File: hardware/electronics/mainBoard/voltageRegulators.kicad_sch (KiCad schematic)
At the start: 46 parts, among them U16 TPS543B25, U17 TPS62A01, U18 TPS62A01, U19 TPS629206

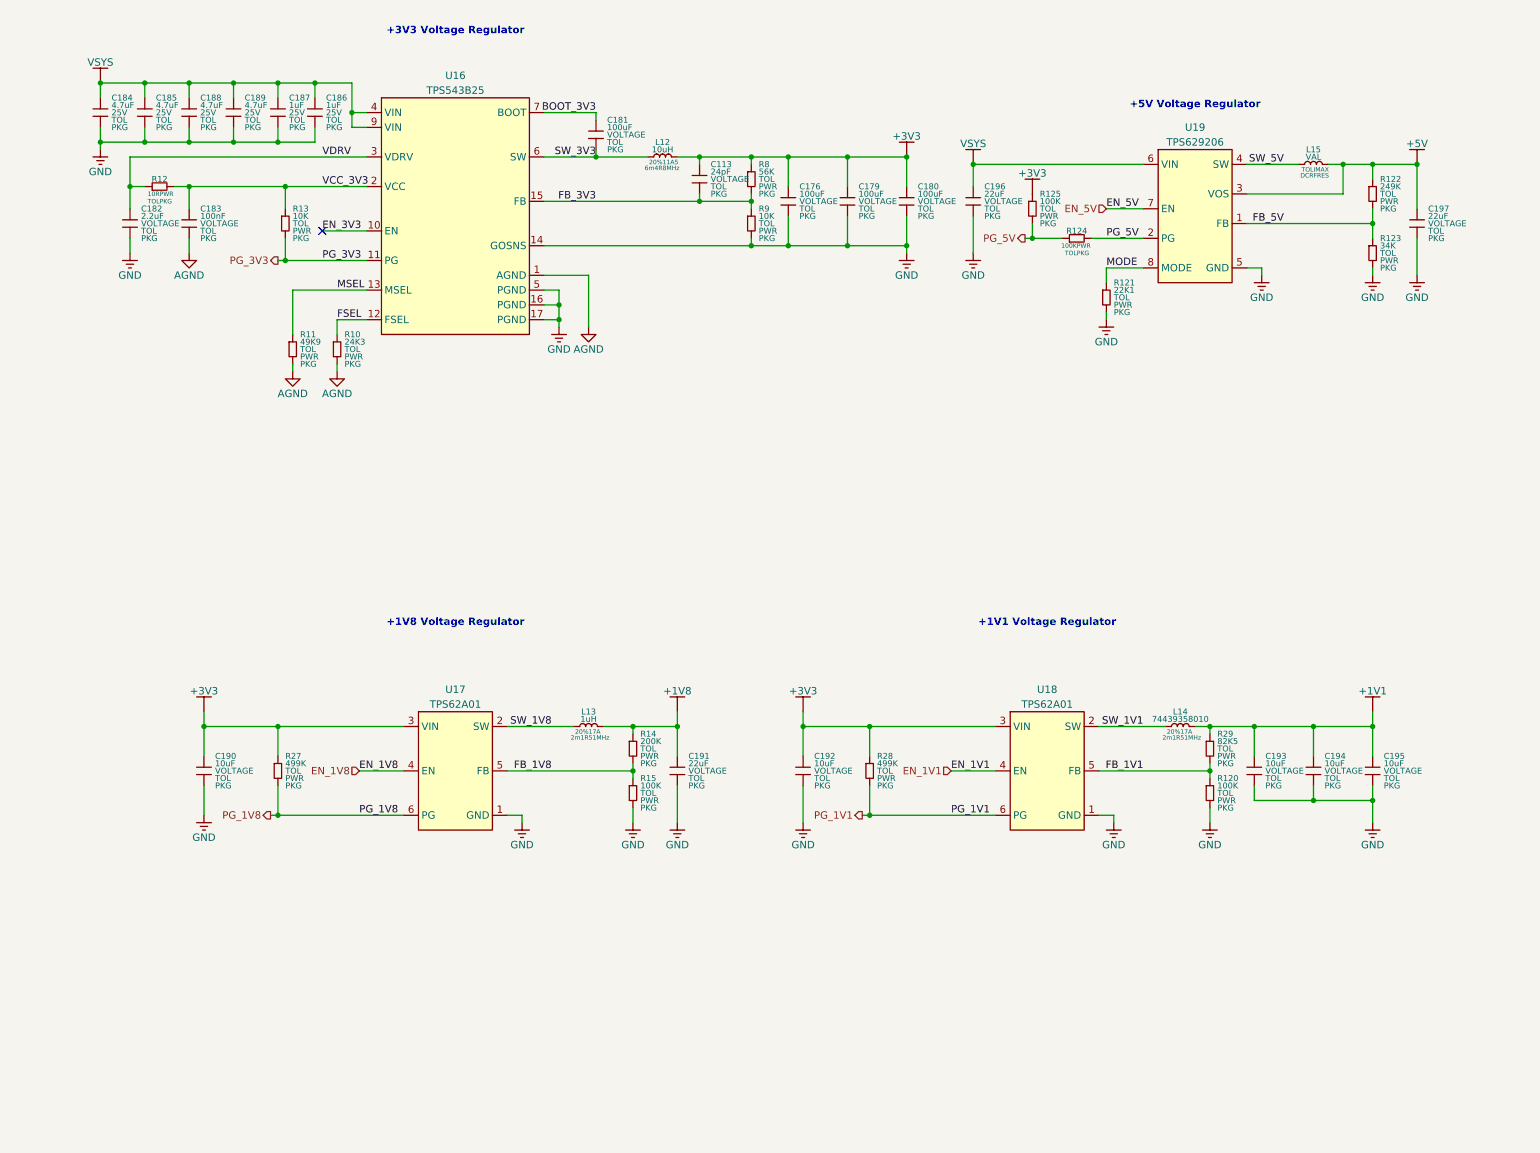
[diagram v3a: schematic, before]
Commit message: added part numbers and stuff
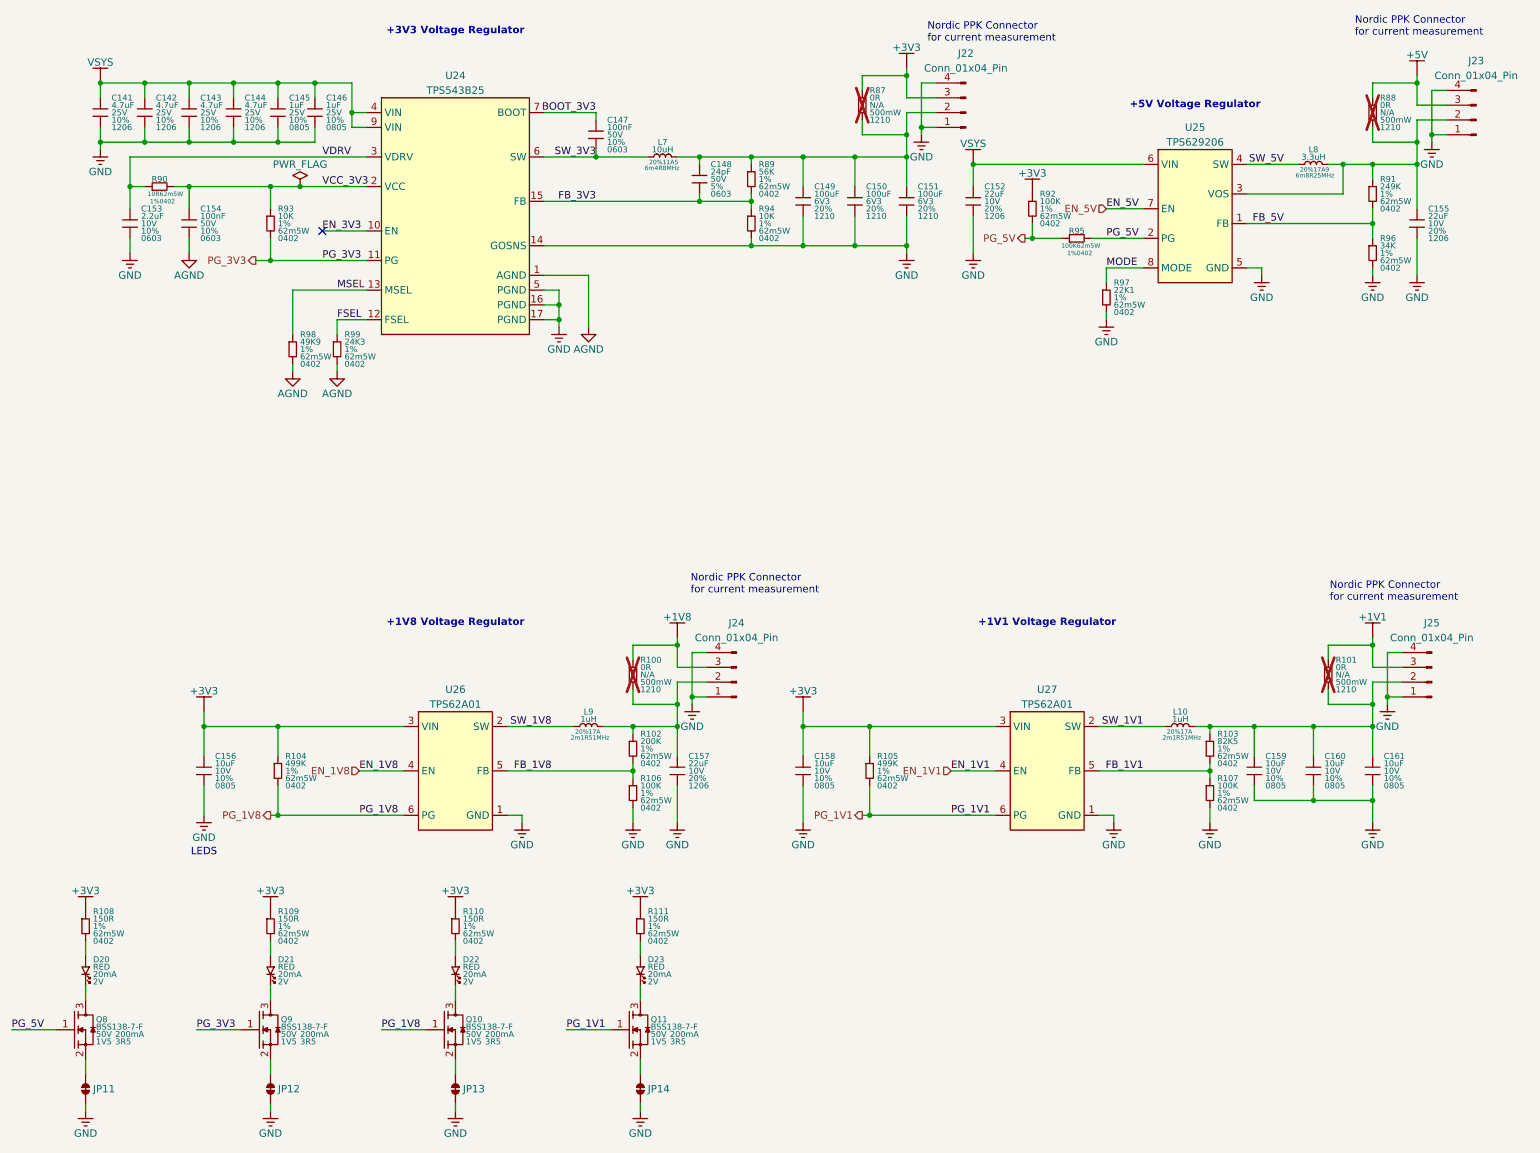
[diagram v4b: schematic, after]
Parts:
- removed C179, C180, C181: 100uF, symbol lib_sch:C
- removed C183: 100nF, symbol lib_sch:C
- removed C185, C188, C189: 4.7uF, symbol lib_sch:C
- removed C186: 1uF, symbol lib_sch:C
- removed C190, C192, C193, C194, C195: 10uF, symbol lib_sch:C
- removed C191, C196, C197: 22uF, symbol lib_sch:C
- removed R120, R15: 100K, symbol lib_sch:R
- removed R13, R9: 10K, symbol lib_sch:R
- removed R28: 499K, symbol lib_sch:R
- added C142, C143, C144: 4.7uF, symbol lib_sch:C
- added C146: 1uF, symbol lib_sch:C
- added C147, C154: 100nF, symbol lib_sch:C
- added C150, C151: 100uF, symbol lib_sch:C
- added C152, C155, C157: 22uF, symbol lib_sch:C
- added C156, C158, C159, C160, C161: 10uF, symbol lib_sch:C
- added D20, D21, D22, D23: LTST-C191KRKT, symbol lib_sch:LED
- added J22, J23, J24, J25: Conn_01x04_Pin, symbol lib_sch:Conn_01x04_Pin
- added JP11, JP12, JP13, JP14: ~, symbol lib_sch:Jumper_2_Bridged
- added Q10, Q11, Q8, Q9: BSS138-7-F, symbol .DS-Transistors:NMOS_GSD
- added R100, R101, R87, R88: 0R, symbol lib_sch:R
- added R105: 499K, symbol lib_sch:R
- added R106, R107: 100K, symbol lib_sch:R
- added R108, R109, R110, R111: 150R, symbol lib_sch:R
- added R93, R94: 10K, symbol lib_sch:R
- C141: renamed from C184; DKPN (none) -> 478-KAM31GR71E475KLCT-ND; MPN (none) -> 12063C475K4T4A; Manufacturer (none) -> KYOCERA AVX; Package PKG -> 1206; Tolerance TOL -> 10%
- C145: renamed from C187; DKPN (none) -> 478-KAF21KR71E105KLCT-ND; MPN (none) -> 08053C105K4Z4A; Manufacturer (none) -> KYOCERA AVX; Package PKG -> 0805; Tolerance TOL -> 10%
- C148: renamed from C113; DKPN (none) -> 478-10304-1-ND; MPN (none) -> 06035A240JAT2A; Manufacturer (none) -> KYOCERA AVX; Package PKG -> 0603; Tolerance TOL -> 5%; Voltage Rating VOLTAGE -> 50V
- C149: renamed from C176; DKPN (none) -> 490-GRT32EC70J107ME13LCT-ND; MPN (none) -> GRT32EC70J107ME13L; Manufacturer (none) -> Murata Electronics; Package PKG -> 1210; Tolerance TOL -> 20%; Voltage Rating VOLTAGE -> 6V3
- C153: renamed from C182; DKPN (none) -> 478-KAM15AR71A225KTCT-ND; MPN (none) -> KAM15AR71A225KT; Manufacturer (none) -> KYOCERA AVX; Package PKG -> 0603; Tolerance TOL -> 10%; Voltage Rating VOLTAGE -> 10V
- L10: renamed from L14; value 74439358010 -> 1uH
- L8: renamed from L15; value VAL -> 3.3uH; Current Rating IMAX -> 17A9; DC Resistance DCR -> 6m8R; DKPN (none) -> 732-74439358033CT-ND; MPN (none) -> 74439358033; Manufacturer (none) -> Würth Elektronik; Resonant Frequency FRES -> 25MHz; Tolerance TOL -> 20%
- R102: renamed from R14; DKPN (none) -> 541-200KLCT-ND; MPN (none) -> CRCW0402200KFKED; Manufacturer (none) -> Vishay Dale; Package PKG -> 0402; Power Rating PWR -> 62m5W; Tolerance TOL -> 1%
- R103: renamed from R29; DKPN (none) -> 541-82.5KLCT-ND; MPN (none) -> CRCW040282K5FKED; Manufacturer (none) -> Vishay Dale; Package PKG -> 0402; Power Rating PWR -> 62m5W; Tolerance TOL -> 1%
- R104: renamed from R27; DKPN (none) -> 541-499KLCT-ND; MPN (none) -> CRCW0402499KFKED; Manufacturer (none) -> Vishay Dale; Package PKG -> 0402; Power Rating PWR -> 62m5W; Tolerance TOL -> 1%
- R89: renamed from R8; DKPN (none) -> 541-56.0KLCT-ND; MPN (none) -> CRCW040256K0FKED; Manufacturer (none) -> Vishay Dale; Package PKG -> 0402; Power Rating PWR -> 62m5W; Tolerance TOL -> 1%
- R90: renamed from R12; DKPN (none) -> 541-10.0LCT-ND; MPN (none) -> CRCW040210R0FKED; Manufacturer (none) -> Vishay Dale; Package PKG -> 0402; Power Rating PWR -> 62m5W; Tolerance TOL -> 1%
- R91: renamed from R122; DKPN (none) -> 541-249KLCT-ND; MPN (none) -> CRCW0402249KFKED; Manufacturer (none) -> Vishay Dale; Package PKG -> 0402; Power Rating PWR -> 62m5W; Tolerance TOL -> 1%
- R92: renamed from R125; DKPN (none) -> 541-100KLCT-ND; MPN (none) -> CRCW0402100KFKED; Manufacturer (none) -> Vishay Dale; Package PKG -> 0402; Power Rating PWR -> 62m5W; Tolerance TOL -> 1%
- R95: renamed from R124; DKPN (none) -> 541-100KLCT-ND; MPN (none) -> CRCW0402100KFKED; Manufacturer (none) -> Vishay Dale; Package PKG -> 0402; Power Rating PWR -> 62m5W; Tolerance TOL -> 1%
- R96: renamed from R123; DKPN (none) -> 541-34.0KLCT-ND; MPN (none) -> CRCW040234K0FKED; Manufacturer (none) -> Vishay Dale; Package PKG -> 0402; Power Rating PWR -> 62m5W; Tolerance TOL -> 1%
- R97: renamed from R121; DKPN (none) -> 541-22.1KLCT-ND; MPN (none) -> CRCW040222K1FKED; Manufacturer (none) -> Vishay Dale; Package PKG -> 0402; Power Rating PWR -> 62m5W; Tolerance TOL -> 1%
- R98: renamed from R11; DKPN (none) -> 541-49.9KLCT-ND; MPN (none) -> CRCW040249K9FKED; Manufacturer (none) -> Vishay Dale; Package PKG -> 0402; Power Rating PWR -> 62m5W; Tolerance TOL -> 1%
- R99: renamed from R10; DKPN (none) -> 541-24.3KLCT-ND; MPN (none) -> CRCW040224K3FKED; Manufacturer (none) -> Vishay Dale; Package PKG -> 0402; Power Rating PWR -> 62m5W; Tolerance TOL -> 1%
- U24: renamed from U16; symbol .DS-PMIC:TPS543B25 -> lib_sch:TPS543B25
- U25: renamed from U19; symbol .DS-PMIC:TPS629206 -> lib_sch:TPS629206; DKPN (none) -> 296-TPS629206DRLRCT-ND; MPN (none) -> TPS629206DRLR
- U26: renamed from U17; symbol .DS-PMIC:TPS62A0x -> lib_sch:TPS62A0x
- U27: renamed from U18; symbol .DS-PMIC:TPS62A0x -> lib_sch:TPS62A0x
- renumbered L12 to L7, L13 to L9
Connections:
- net +1V1: now also J25.3 (Pin_3), R101.1; no longer L10.2, R103.1
- net +1V8: now also J24.3 (Pin_3), R100.1; no longer L9.2, R102.1
- net +3V3: now also C156.1, C158.1, J22.3 (Pin_3), R105.1, R108.1, R109.1, R110.1, R111.1, R87.1; no longer C148.1, C149.1, L7.2, R89.1
- net +5V: now also J23.3 (Pin_3), R88.1; no longer L8.2, R91.1, U25.3 (VOS)
- net AGND: now also C154.2
- net BOOT_3V3: now also C147.1
- net FB_1V1: now also R107.1
- net FB_1V8: now also R106.1
- net FB_3V3: now also R94.1
- net GND: now also C142.2, C143.2, C144.2, C146.2, C150.2, C151.2, C152.2, C155.2, C156.2, C157.2, C158.2, C159.2, C160.2, C161.2, J22.1 (Pin_1), J22.4 (Pin_4), J23.1 (Pin_1), J23.4 (Pin_4), J24.1 (Pin_1), J24.4 (Pin_4), J25.1 (Pin_1), J25.4 (Pin_4), JP11.2, JP12.2, JP13.2, JP14.2, R106.2, R107.2, R94.2
- net PG_1V1: now also Q11.1, R105.2
- net PG_1V8: now also Q10.1
- net PG_3V3: now also Q9.1, R93.2
- net PG_5V: now also Q8.1
- net SW_3V3: now also C147.2
- net VCC_3V3: now also C154.1, R93.1
- net VSYS: now also C142.1, C143.1, C144.1, C146.1, C152.1
- new net: D22.1, R110.2
- new net: D22.2, Q10.3
- new net: C155.1, J23.2 (Pin_2), L8.2, R88.2, R91.1, U25.3 (VOS)
- new net: C159.1, C160.1, C161.1, J25.2 (Pin_2), L10.2, R101.2, R103.1
- new net: C148.1, C149.1, C150.1, C151.1, J22.2 (Pin_2), L7.2, R87.2, R89.1
- new net: JP14.1, Q11.2
- new net: C157.1, J24.2 (Pin_2), L9.2, R100.2, R102.1
- new net: D21.1, R109.2
- new net: D21.2, Q9.3
- new net: JP13.1, Q10.2
- new net: JP12.1, Q9.2
- new net: D20.1, R108.2
- new net: D20.2, Q8.3
- new net: D23.2, Q11.3
- new net: JP11.1, Q8.2
- new net: D23.1, R111.2
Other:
- note added: "LEDS"
- note added: "Nordic PPK Connector for current measurement"
- moved on the sheet: C149

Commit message: got rid of 5V and 1V1 regs
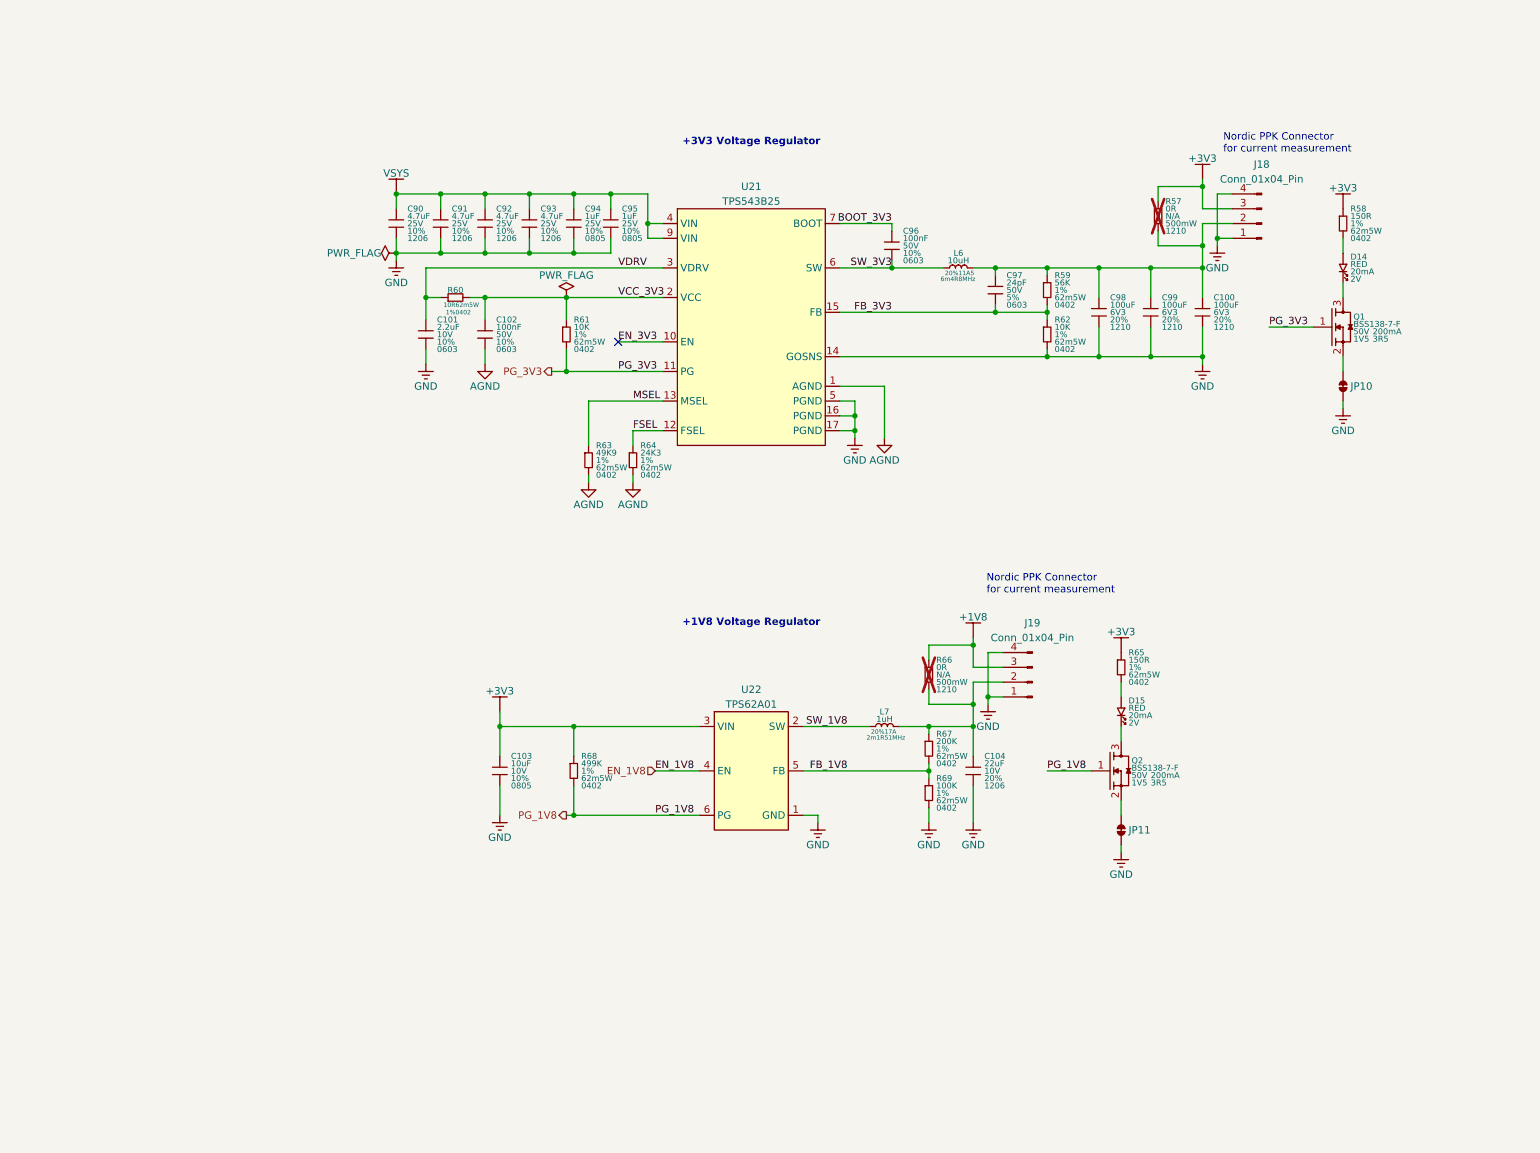
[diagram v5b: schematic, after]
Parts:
- removed C152, C155: 22uF, symbol lib_sch:C
- removed C158, C159, C160, C161: 10uF, symbol lib_sch:C
- removed D20, D23: LTST-C191KRKT, symbol lib_sch:LED
- removed J23, J24, J25: Conn_01x04_Pin, symbol lib_sch:Conn_01x04_Pin
- removed JP11, JP14: ~, symbol lib_sch:Jumper_2_Bridged
- removed L10: 1uH, symbol lib_sch:L_horizontal
- removed L8: 3.3uH, symbol lib_sch:L_horizontal
- removed Q11, Q8: BSS138-7-F, symbol .DS-Transistors:NMOS_GSD
- removed R101, R88: 0R, symbol lib_sch:R
- removed R103: 82K5, symbol lib_sch:R
- removed R105: 499K, symbol lib_sch:R
- removed R107, R92: 100K, symbol lib_sch:R
- removed R108, R111: 150R, symbol lib_sch:R
- removed R91: 249K, symbol lib_sch:R
- removed R95: 100K, symbol lib_sch:R_horizontal
- removed R96: 34K, symbol lib_sch:R
- removed R97: 22K1, symbol lib_sch:R
- removed U25: TPS629206, symbol lib_sch:TPS629206
- removed U27: TPS62A01, symbol lib_sch:TPS62A0x
- added J19: Conn_01x04_Pin, symbol lib_sch:Conn_01x04_Pin
- renumbered C151 to C100, C153 to C101, C154 to C102, C156 to C103, C157 to C104, C141 to C90, C142 to C91, C143 to C92, C144 to C93, C145 to C94, C146 to C95, C147 to C96, C148 to C97, C149 to C98, C150 to C99, D21 to D14, D22 to D15, J22 to J18, JP12 to JP10, JP13 to JP11, L7 to L6, L9 to L7, Q9 to Q1, Q10 to Q2, R87 to R57, R109 to R58, R89 to R59, R90 to R60, R93 to R61, R94 to R62, R98 to R63, R99 to R64, R110 to R65, R100 to R66, R102 to R67, R104 to R68, R106 to R69, U24 to U21, U26 to U22
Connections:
- net +1V8: now also J19.3 (Pin_3)
- net GND: now also J19.1 (Pin_1), J19.4 (Pin_4)
- net at C104.1, L7.2, R66.2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: now also J19.2 (Pin_2)
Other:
- note removed: "+1V1 Voltage Regulator"
- note removed: "+5V Voltage Regulator"
- note removed: "LEDS"
- moved on the sheet: C100, C101, C102, C103, C104, C90, C91, C92, C93, C94, C95, C96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

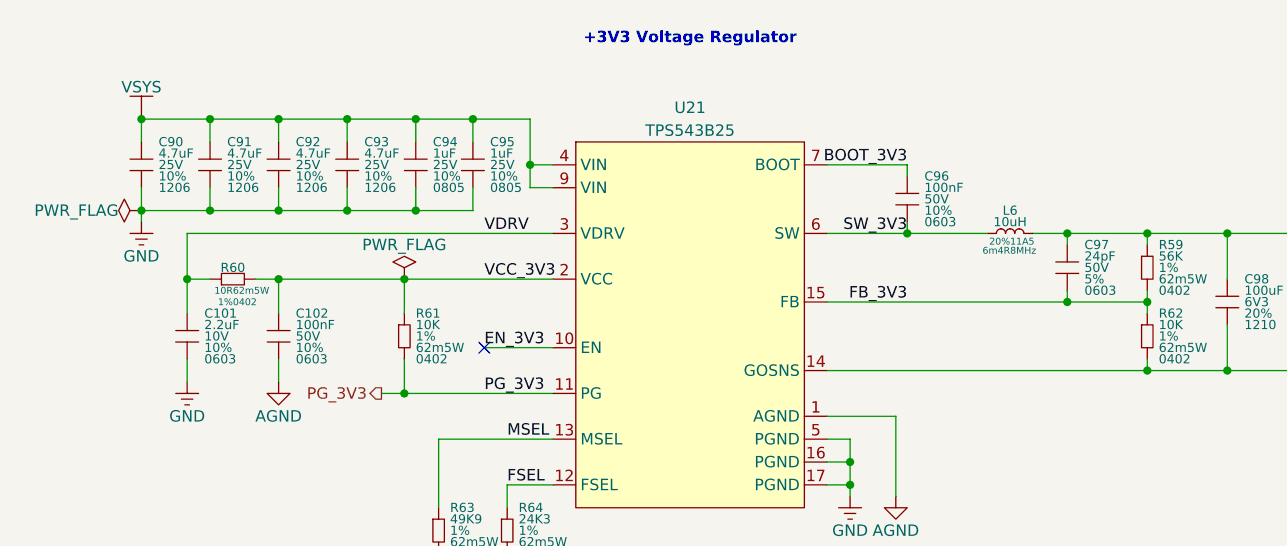
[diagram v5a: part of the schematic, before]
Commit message: updated capacitors
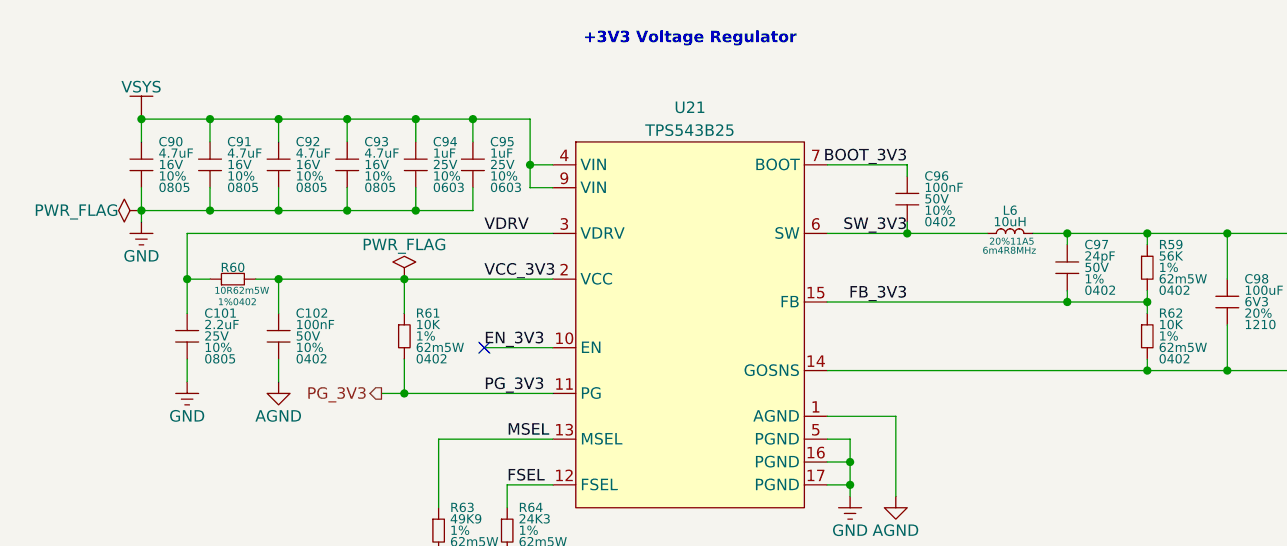
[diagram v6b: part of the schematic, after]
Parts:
- C101: DKPN 478-KAM15AR71A225KTCT-ND -> 490-GRT21BR71E225KE13LCT-ND; MPN KAM15AR71A225KT -> GRT21BR71E225KE13L; Manufacturer KYOCERA AVX -> Murata Electronics; Package 0603 -> 0805; Voltage Rating 10V -> 25V
- C102, C96: DKPN 478-KAM15AR71H104KTCT-ND -> 490-GRT155R71H104KE01DCT-ND; MPN 06035C104K4T2A -> GRT155R71H104KE01D; Manufacturer KYOCERA AVX -> Murata Electronics; Package 0603 -> 0402
- C103: DKPN 478-KAM21AR71A106KUCT-ND -> 490-10674-1-ND; MPN KAM21AR71A106KU -> GCM21BR71A106KE22L; Manufacturer KYOCERA AVX -> Murata Electronics
- C90, C91, C92, C93: DKPN 478-KAM31GR71E475KLCT-ND -> 490-GRT21BR71C475KE13LCT-ND; MPN 12063C475K4T4A -> GRT21BR71C475KE13L; Manufacturer KYOCERA AVX -> Murata Electronics; Package 1206 -> 0805; Voltage Rating 25V -> 16V
- C94, C95: DKPN 478-KAF21KR71E105KLCT-ND -> 490-GRT188R71E105KE13DCT-ND; MPN 08053C105K4Z4A -> GRT188R71E105KE13D; Manufacturer KYOCERA AVX -> Murata Electronics; Package 0805 -> 0603
- C97: DKPN 478-10304-1-ND -> 490-GCM1555C1H240FA16DCT-ND; MPN 06035A240JAT2A -> GCM1555C1H240FA16D; Manufacturer KYOCERA AVX -> Murata Electronics; Package 0603 -> 0402; Tolerance 5% -> 1%
